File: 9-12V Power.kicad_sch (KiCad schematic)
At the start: 1 part, among them U5 TPS54540BDDA

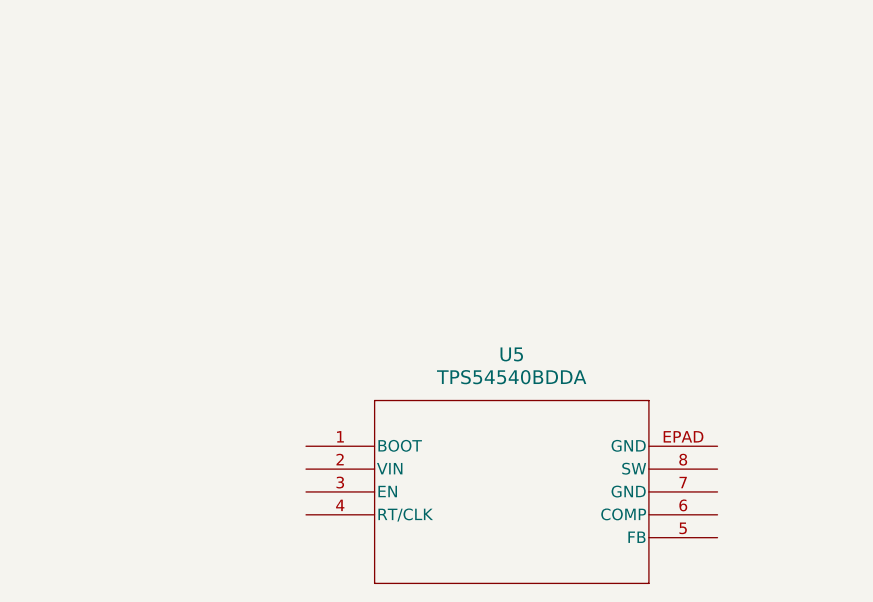
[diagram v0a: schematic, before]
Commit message: Updates to the 5V buck converter
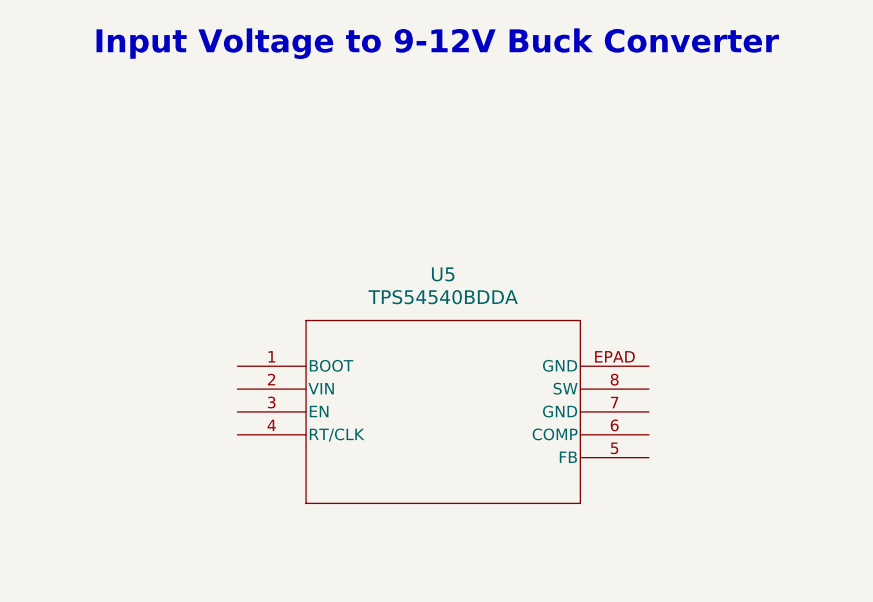
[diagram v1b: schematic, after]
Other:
- note added: "Input Voltage to 9-12V Buck Converter"
- moved on the sheet: U5
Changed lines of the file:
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@@
 		(title "9-12V Power")
+	)
+	(text "Input Voltage to 9-12V Buck Converter"
+		(exclude_from_sim no)
+		(at 137.668 53.086 0)
+		(effects
+			(font
+				(size 2.54 2.54)
+				(thickness 0.508)
+				(bold yes)
+			)
+		)
 	)
 	(symbol
 		(lib_id "2026-07-22_15-59-22:TPS54540BDDA")
-		(at 123.19 97.79 0)
+		(at 115.57 88.9 0)
 		(unit 1)
 		(body_style 1)
@@
 		(fields_autoplaced yes)
 		(property "Reference" "U5"
-			(at 146.05 87.63 0)
+			(at 138.43 78.74 0)
 			(show_name no)
 			(do_not_autoplace no)
@@
 		)
 		(property "Value" "TPS54540BDDA"
-			(at 146.05 90.17 0)
+			(at 138.43 81.28 0)
 			(show_name no)
 			(do_not_autoplace no)
@@
 		)
 		(property "Footprint" "SO-POWERPAD8_DDA_TEX"
-			(at 123.19 97.79 0)
+			(at 115.57 88.9 0)
 			(hide yes)
 			(show_name no)
@@
 		)
 		(property "Datasheet" "https://www.ti.com/lit/gpn/tps54540b"
-			(at 123.19 97.79 0)
+			(at 115.57 88.9 0)
 			(hide yes)
 			(show_name no)
@@
 		)
 		(property "Description" ""
-			(at 123.19 97.79 0)
+			(at 115.57 88.9 0)
 			(hide yes)
 			(show_name no)

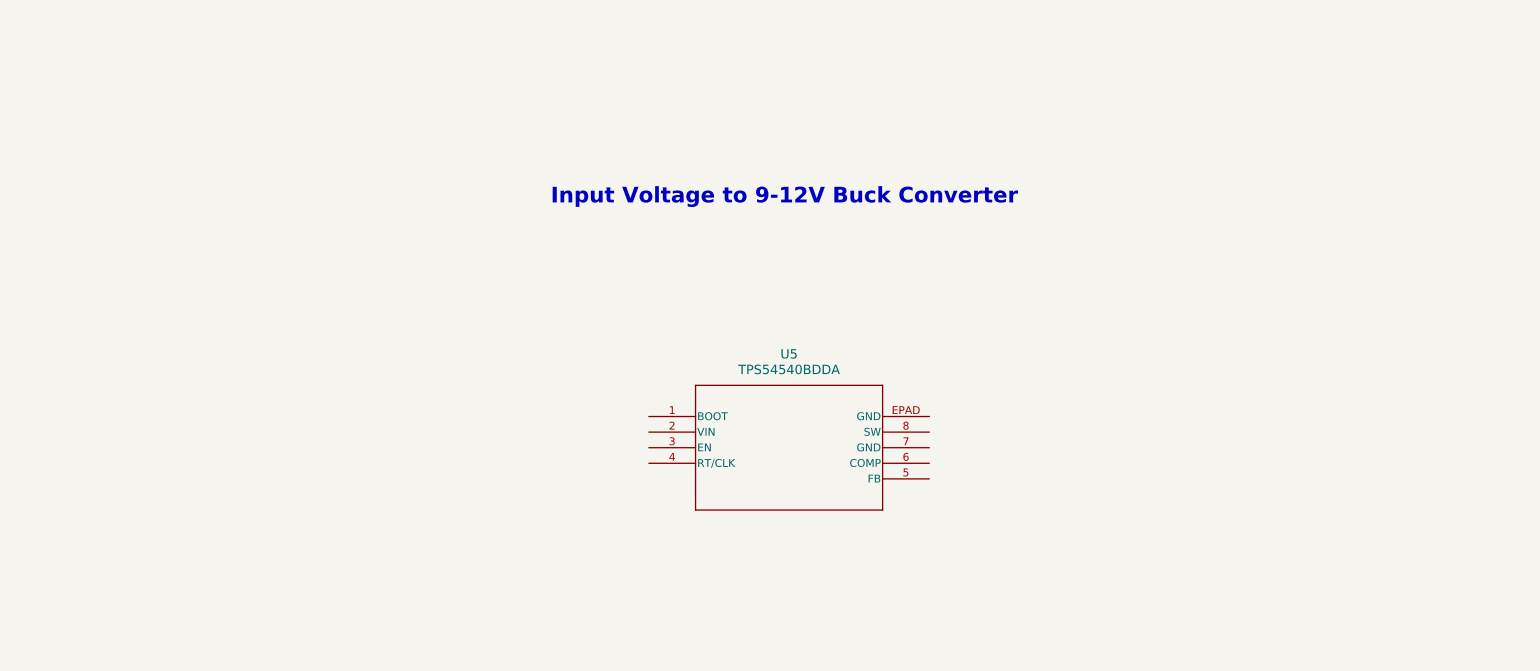
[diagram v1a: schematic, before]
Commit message: Added new potentiometer
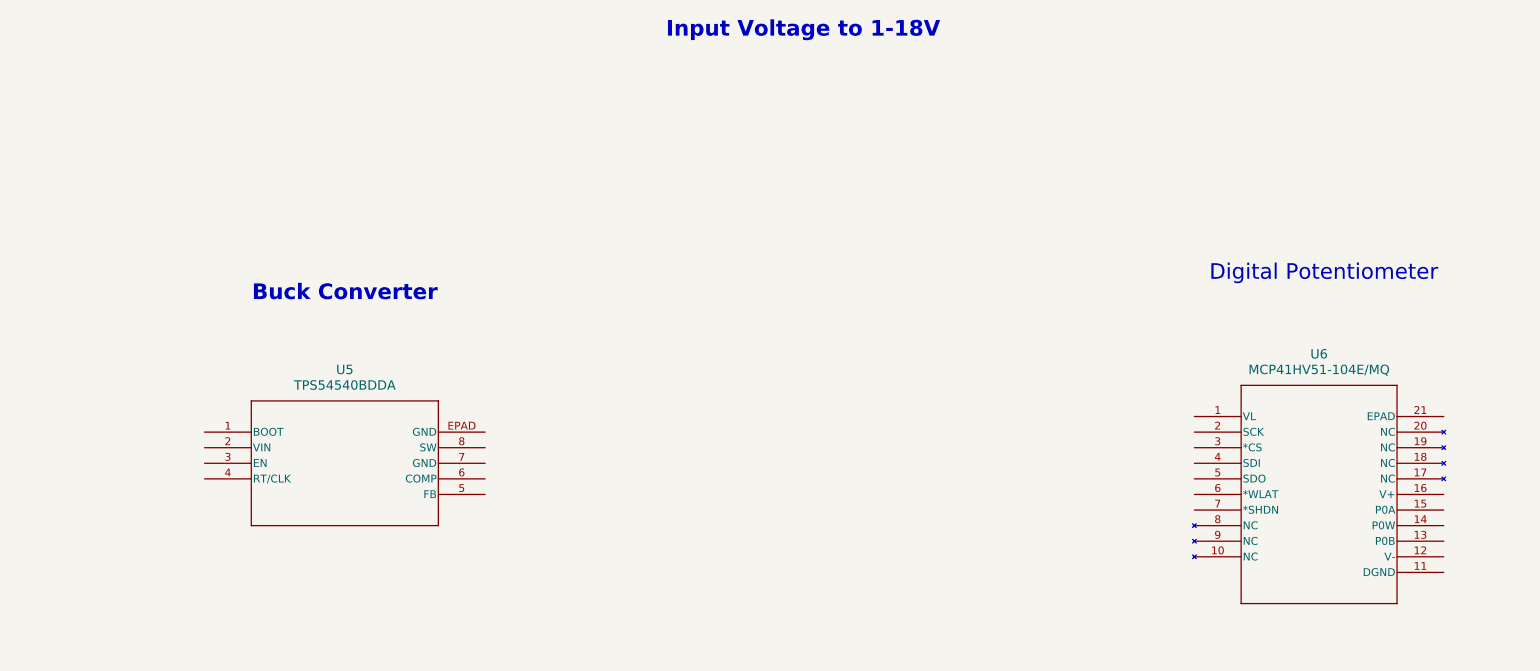
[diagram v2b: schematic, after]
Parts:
- added U6: MCP41HV51-104E/MQ, QFN20_5x5MC_MCH, symbol 2026-09-23_13-25-41:MCP41HV51-104E_MQ
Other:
- note added: "Buck Converter"
- note added: "Digital Potentiometer"
- note added: "Input Voltage to 1-18V"
- note removed: "Input Voltage to 9-12V Buck Converter"
- title: 9-12V Power -> 1-18V Power
- moved on the sheet: U5
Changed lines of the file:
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@@
 	(paper "A4")
 	(title_block
-		(title "9-12V Power")
-	)
-	(text "Input Voltage to 9-12V Buck Converter"
-		(exclude_from_sim no)
-		(at 137.668 53.086 0)
+		(title "1-18V Power")
+	)
+	(text "Input Voltage to 1-18V"
+		(exclude_from_sim no)
+		(at 140.716 25.908 0)
 		(effects
 			(font
@@
 		)
 	)
+	(text "Digital Potentiometer"
+		(exclude_from_sim no)
+		(at 225.552 65.532 0)
+		(effects
+			(font
+				(size 2.54 2.54)
+				(thickness 0.3175)
+			)
+		)
+	)
+	(text ""
+		(exclude_from_sim no)
+		(at 226.822 66.04 0)
+		(effects
+			(font
+				(size 2.54 2.54)
+				(thickness 0.254)
+				(bold yes)
+			)
+		)
+	)
+	(text "Buck Converter"
+		(exclude_from_sim no)
+		(at 66.04 68.834 0)
+		(effects
+			(font
+				(size 2.54 2.54)
+				(thickness 0.254)
+				(bold yes)
+			)
+		)
+	)
 	(symbol
 		(lib_id "2026-07-22_15-59-22:TPS54540BDDA")
-		(at 115.57 88.9 0)
+		(at 43.18 91.44 0)
 		(unit 1)
 		(body_style 1)
@@
 		(fields_autoplaced yes)
 		(property "Reference" "U5"
-			(at 138.43 78.74 0)
+			(at 66.04 81.28 0)
 			(show_name no)
 			(do_not_autoplace no)
@@
 		)
 		(property "Value" "TPS54540BDDA"
-			(at 138.43 81.28 0)
+			(at 66.04 83.82 0)
 			(show_name no)
 			(do_not_autoplace no)
@@
 		)
 		(property "Footprint" "SO-POWERPAD8_DDA_TEX"
-			(at 115.57 88.9 0)
+			(at 43.18 91.44 0)
 			(hide yes)
 			(show_name no)
@@
 		)
 		(property "Datasheet" "https://www.ti.com/lit/gpn/tps54540b"
-			(at 115.57 88.9 0)
+			(at 43.18 91.44 0)
 			(hide yes)
 			(show_name no)
@@
 		)
 		(property "Description" ""
-			(at 115.57 88.9 0)
+			(at 43.18 91.44 0)
 			(hide yes)
 			(show_name no)
@@
 					(unit 1)
 				)
+			)
+		)
+	)
+	(symbol
+		(lib_id "2026-09-23_13-25-41:MCP41HV51-104E_MQ")
+		(at 204.47 88.9 0)
+		(unit 1)
+		(body_style 1)
+		(exclude_from_sim no)
+		(in_bom yes)
+		(on_board yes)
+		(in_pos_files yes)
+		(dnp no)
+		(fields_autoplaced yes)
+		(property "Reference" "U6"
+			(at 224.79 78.74 0)
+			(show_name no)
+			(do_not_autoplace no)
+			(effects
+				(font
+					(size 1.524 1.524)
+				)
+			)
+		)
+		(property "Value" "MCP41HV51-104E/MQ"
+			(at 224.79 81.28 0)
+			(show_name no)
+			(do_not_autoplace no)
+			(effects
+				(font
+					(size 1.524 1.524)
+				)
+			)
+		)
+		(property "Footprint" "QFN20_5x5MC_MCH"
+			(at 204.47 88.9 0)
+			(hide yes)
+			(show_name no)
+			(do_not_autoplace no)
+			(effects
+				(font
+					(size 1.27 1.27)
+					(italic yes)
+				)
+			)
+		)
+		(property "Datasheet" "MCP41HV51-104E/MQ"
+			(at 204.47 88.9 0)
+			(hide yes)
+			(show_name no)
+			(do_not_autoplace no)
+			(effects
+				(font
+					(size 1.27 1.27)
+					(italic yes)
+				)
+			)
+		)
+		(property "Description" ""
+			(at 204.47 88.9 0)
+			(hide yes)
+			(show_name no)
+			(do_not_autoplace no)
+			(effects
+				(font
+					(size 1.27 1.27)
+				)
+			)
+		)
+		(pin "13"
+		)
+		(pin "8"
+		)
+		(pin "21"
+		)
+		(pin "7"
+		)
+		(pin "4"
+		)
+		(pin "9"
+		)
+		(pin "11"
+		)
+		(pin "2"
+		)
+		(pin "3"
+		)
+		(pin "14"
+		)
+		(pin "1"
+		)
+		(pin "6"
+		)
+		(pin "12"
+		)
+		(pin "10"
+		)
+		(pin "5"
+		)
+		(pin "15"
+		)
+		(pin "16"
+		)
+		(pin "17"
+		)
+		(pin "18"
+		)
+		(pin "19"
+		)
+		(pin "20"
+		)
+		(instances
+			(project "LEOS-F26-power"
+				(path "/3703ddf2-8141-438d-86a8-1eaec9672d0d/64f3d4b9-893f-4f0f-938c-0da76e19fc55"
+					(reference "U6")
+					(unit 1)
+				)

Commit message: updates to potentiometer
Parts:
- added C10, C11, C12, C13, C14, C15, C16, C17, C8, C9: C, symbol Device:C
- added D1: D_Schottky, symbol Device:D_Schottky
- added L1: L, symbol Device:L
- added R2, R3, R4, R5, R6, R7: R, symbol Device:R
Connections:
- net at U5.1 (BOOT): now also C8.2
- net VIN: now reaches U5.2 (VIN)
- net VIN: now also U6.16 (V+), C10.1, C11.1, C12.1, C9.1, R2.1
- net at U5.3 (EN): now also R2.2, R3.1
- net at U5.4 (RT/CLK): now also R4.1
- net GND: now reaches U5.5 (FB)
- net GND: now also U5.EPAD (GND), U6.11 (DGND), U6.12 (V-), U6.13 (P0B), U6.14 (P0W), U6.21 (EPAD), U6.6 (*WLAT), C10.2, C11.2, C12.2, C15.2, C16.2, C17.2, C9.2, R3.2, R4.2, R7.2
- net at U5.6 (COMP): now also C16.1, R5.1
- net at U5.7 (GND): now also C13.2, C14.2, D1.2 (A)
- net at U5.8 (SW): now also C8.1, D1.1 (K), L1.1
- net VDD: now reaches U6.1 (VL)
- net VDD: now also U6.7 (*SHDN), C17.1
- net SCK1: now reaches U6.2 (SCK)
- net CS1: now reaches U6.3 (*CS)
- net MOSI1: now reaches U6.4 (SDI)
- net MISO1: now reaches U6.5 (SDO)
- new net: C13.1, C14.1, L1.2, R6.1
- new net: C15.1, R5.2
- new net: R6.2, R7.1
- no-connect marks 0 -> 1
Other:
- moved on the sheet: U5, U6

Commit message: added footprints
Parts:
- C-1: renamed from C12; value C -> 4.7u; footprint (none) -> Capacitor_SMD:C_0805_2012Metric
- C-10: renamed from C17; value C -> 0.1u; footprint (none) -> Capacitor_SMD:C_0805_2012Metric
- C-2: renamed from C11; value C -> 4.7u; footprint (none) -> Capacitor_SMD:C_0805_2012Metric
- C-3: renamed from C10; value C -> 4.7u; footprint (none) -> Capacitor_SMD:C_0805_2012Metric
- C-4: renamed from C9; value C -> 4.7u; footprint (none) -> Capacitor_SMD:C_0805_2012Metric
- C-5: renamed from C8; value C -> 100n; footprint (none) -> Capacitor_SMD:C_0805_2012Metric
- C-6: renamed from C15; value C -> 620p; footprint (none) -> Capacitor_SMD:C_0805_2012Metric
- C-7: renamed from C16; value C -> 6.8p; footprint (none) -> Capacitor_SMD:C_0805_2012Metric
- C-8: renamed from C13; value C -> 47u; footprint (none) -> Capacitor_SMD:C_0805_2012Metric
- C-9: renamed from C14; value C -> 47u; footprint (none) -> Capacitor_SMD:C_0805_2012Metric
- D-1: renamed from D1; value D_Schottky -> 560m; footprint (none) -> Diode_SMD:D_0805_2012Metric
- L-1: renamed from L1; value L -> 10u; footprint (none) -> Inductor_SMD:L_0805_2012Metric
- R-1: renamed from R2; value R -> 365k; footprint (none) -> Resistor_SMD:R_0805_2012Metric
- R-2: renamed from R3; value R -> 88.7; footprint (none) -> Resistor_SMD:R_0805_2012Metric
- R-3: renamed from R4; value R -> 133k; footprint (none) -> Resistor_SMD:R_0805_2012Metric
- R-4: renamed from R5; value R -> 56.2k; footprint (none) -> Resistor_SMD:R_0805_2012Metric
- R-5: renamed from R7; value R -> 1.1k; footprint (none) -> Resistor_SMD:R_0805_2012Metric
- R-6: renamed from R6; value R -> 25.5k; footprint (none) -> Resistor_SMD:R_0805_2012Metric
- U5: footprint SO-POWERPAD8_DDA_TEX -> (none)
- U6: footprint QFN20_5x5MC_MCH -> (none)

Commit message: testing
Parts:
- C-1, C-2, C-3, C-4: Digikey (none) -> 1276-2970-1-ND; MPN (none) -> CL21B475KOFNFNE; Manufacturer (none) -> Samsung Electro-Mechanics
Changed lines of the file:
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@@
+			)
+		)
+		(property "Digikey" "1276-2970-1-ND"
+			(at 27.94 97.79 0)
+			(hide yes)
+			(show_name no)
+			(do_not_autoplace no)
+			(effects
+				(font
+					(size 1.27 1.27)
+				)
+			)
+		)
+		(property "MPN" "CL21B475KOFNFNE"
+			(at 27.94 97.79 0)
+			(hide yes)
+			(show_name no)
+			(do_not_autoplace no)
+			(effects
+				(font
+					(size 1.27 1.27)
+				)
+			)
+		)
+		(property "Manufacturer" "Samsung Electro-Mechanics"
+			(at 27.94 97.79 0)
+			(hide yes)
+			(show_name no)
+			(do_not_autoplace no)
+			(effects
+				(font
+					(size 1.27 1.27)
+				)
 			)
 		)
@@
 			)
 		)
+		(property "Digikey" "1276-2970-1-ND"
+			(at 21.59 97.79 0)
+			(hide yes)
+			(show_name no)
+			(do_not_autoplace no)
+			(effects
+				(font
+					(size 1.27 1.27)
+				)
+			)
+		)
+		(property "MPN" "CL21B475KOFNFNE"
+			(at 21.59 97.79 0)
+			(hide yes)
+			(show_name no)
+			(do_not_autoplace no)
+			(effects
+				(font
+					(size 1.27 1.27)
+				)
+			)
+		)
+		(property "Manufacturer" "Samsung Electro-Mechanics"
+			(at 21.59 97.79 0)
+			(hide yes)
+			(show_name no)
+			(do_not_autoplace no)
+			(effects
+				(font
+					(size 1.27 1.27)
+				)
+			)
+		)
 		(pin "1"
 		)
@@
 		)
 		(property "Description" "Unpolarized capacitor"
+			(at 40.64 97.79 0)
+			(hide yes)
+			(show_name no)
+			(do_not_autoplace no)
+			(effects
+				(font
+					(size 1.27 1.27)
+				)
+			)
+		)
+		(property "Digikey" "1276-2970-1-ND"
+			(at 40.64 97.79 0)
+			(hide yes)
+			(show_name no)
+			(do_not_autoplace no)
+			(effects
+				(font
+					(size 1.27 1.27)
+				)
+			)
+		)
+		(property "MPN" "CL21B475KOFNFNE"
+			(at 40.64 97.79 0)
+			(hide yes)
+			(show_name no)
+			(do_not_autoplace no)
+			(effects
+				(font
+					(size 1.27 1.27)
+				)
+			)
+		)
+		(property "Manufacturer" "Samsung Electro-Mechanics"
 			(at 40.64 97.79 0)
 			(hide yes)
@@
 			(at 34.29 97.79 0)
 			(hide yes)
+			(show_name no)
+			(do_not_autoplace no)
+			(effects
+				(font
+					(size 1.27 1.27)
+				)
+			)
+		)
+		(property "Digikey" "1276-2970-1-ND"
+			(at 34.29 97.79 0)
+			(hide yes)
+			(show_name no)
+			(do_not_autoplace no)
+			(effects
+				(font
+					(size 1.27 1.27)
+				)
+			)
+		)
+		(property "MPN" "CL21B475KOFNFNE"
+			(at 34.29 97.79 0)
+			(hide yes)
+			(show_name no)
+			(do_not_autoplace no)
+			(effects
+				(font
+					(size 1.27 1.27)
+				)
+			)
+		)
+		(property "Manufacturer" "Samsung Electro-Mechanics"
+			(at 34.29 97.79 0)
+			(hide yes)

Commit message: updating
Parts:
- C-6: Digikey (none) -> 490-1618-1-ND; MPN (none) -> GRM2165C1H621JA01D; Manufacturer (none) -> Murata Electronics
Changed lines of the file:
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@@
+			)
+		)
+		(property "Digikey" "490-1618-1-ND"
+			(at 110.49 113.03 0)
+			(hide yes)
+			(show_name no)
+			(do_not_autoplace no)
+			(effects
+				(font
+					(size 1.27 1.27)
+				)
+			)
+		)
+		(property "MPN" "GRM2165C1H621JA01D"
+			(at 110.49 113.03 0)
+			(hide yes)
+			(show_name no)
+			(do_not_autoplace no)
+			(effects
+				(font
+					(size 1.27 1.27)
+				)
+			)
+		)
+		(property "Manufacturer" "Murata Electronics"
+			(at 110.49 113.03 0)
+			(hide yes)
+			(show_name no)
+			(do_not_autoplace no)
+			(effects
+				(font
+					(size 1.27 1.27)
+				)
 			)
 		)

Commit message: capacitor
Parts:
- C-10: Digikey (none) -> 1276-1003-1-ND; LCSC (none) -> C1711; MPN (none) -> CL21B104KBCNNNC; Manufacturer (none) -> Samsung Electro-Mechanics
- C-7: Digikey (none) -> 399-C0805C689C3HACAUTOCT-ND; MPN (none) -> C0805C689C3HACAUTO; Manufacturer (none) -> KEMET
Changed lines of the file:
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@@
+			)
+		)
+		(property "Digikey" "399-C0805C689C3HACAUTOCT-ND"
+			(at 120.65 104.14 0)
+			(hide yes)
+			(show_name no)
+			(do_not_autoplace no)
+			(effects
+				(font
+					(size 1.27 1.27)
+				)
+			)
+		)
+		(property "MPN" "C0805C689C3HACAUTO"
+			(at 120.65 104.14 0)
+			(hide yes)
+			(show_name no)
+			(do_not_autoplace no)
+			(effects
+				(font
+					(size 1.27 1.27)
+				)
+			)
+		)
+		(property "Manufacturer" "KEMET"
+			(at 120.65 104.14 0)
+			(hide yes)
+			(show_name no)
+			(do_not_autoplace no)
+			(effects
+				(font
+					(size 1.27 1.27)
+				)
 			)
 		)
@@
 			)
 		)
-		(property "Description" "Unpolarized capacitor"
+		(property "Description" "0.1uF 50V X7R 0805"
 			(at 179.07 80.01 0)
 			(hide yes)
+			(show_name no)
+			(do_not_autoplace no)
+			(effects
+				(font
+					(size 1.27 1.27)
+				)
+			)
+		)
+		(property "Digikey" "1276-1003-1-ND"
+			(at 179.07 80.01 0)
+			(hide yes)
+			(show_name no)
+			(do_not_autoplace no)
+			(effects
+				(font
+					(size 1.27 1.27)
+				)
+			)
+		)
+		(property "LCSC" "C1711"
+			(at 179.07 80.01 0)
+			(hide yes)
+			(show_name no)
+			(do_not_autoplace no)
+			(effects
+				(font
+					(size 1.27 1.27)
+				)
+			)
+		)
+		(property "MPN" "CL21B104KBCNNNC"
+			(at 179.07 80.01 0)
+			(hide yes)
+			(show_name no)
+			(do_not_autoplace no)
+			(effects
+				(font
+					(size 1.27 1.27)
+				)
+			)
+		)
+		(property "Manufacturer" "Samsung Electro-Mechanics"
+			(at 179.07 80.01 0)
+			(hide yes)
